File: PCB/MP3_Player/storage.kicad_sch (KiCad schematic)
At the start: 8 parts, among them J6 Micro_SD_Card

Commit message: Minor Schematic Changes
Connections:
- net DAT1: now also R19.2; no longer R17.2
- net DAT2: now also R17.2; no longer R19.2
- net SD_CMD: now also R20.1; no longer R21.1
- net SD_DAT0: now also R21.1; no longer R20.1
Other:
- moved on the sheet: C35, C36

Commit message: Started Making BOM
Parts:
- C35: Mfr. Part # (none) -> CL10A106KP8NNNC; Store URL - Digikey (none) -> https://www.digikey.pt/pt/products/detail/samsung-electro-m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; Store URL - Mouser (none) -> https://pt.mouser.com/en/ProductDetail/Samsung-Electro-Mech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
- C36: Mfr. Part # (none) -> CL05B104KP5NNNC; Store URL - Digikey (none) -> https://www.digikey.pt/pt/products/detail/samsung-electro-m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; Store URL - Mouser (none) -> https://pt.mouser.com/en/ProductDetail/Samsung-Electro-Mech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

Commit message: Continue Making BOM
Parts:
- R17, R18, R19, R20, R21: Mfr. Part # (none) -> CRCW040210K0FKED; Store URL - Digikey (none) -> https://www.digikey.pt/pt/products/detail/vishay-dale/CRCW0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; Store URL - Mouser (none) -> https://pt.mouser.com/en/ProductDetail/Vishay/CRCW040210K0F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
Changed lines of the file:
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@@
 			)
 		)
-		(property "Datasheet" ""
+		(property "Datasheet" "https://www.vishay.com/docs/20035/dcrcwe3.pdf"
 			(at 127 97.79 0)
 			(hide yes)
@@
 			)
 		)
-		(property "Description" "Resistor"
+		(property "Description" "0402"
 			(at 127 97.79 0)
 			(hide yes)
@@
 		)
 		(property "Store URL - TME" ""
+			(at 127 97.79 0)
+			(hide yes)
+			(show_name no)
+			(do_not_autoplace no)
+			(effects
+				(font
+					(size 1.27 1.27)
+				)
+			)
+		)
+		(property "Mfr. Part #" "CRCW040210K0FKED"
+			(at 127 97.79 0)
+			(hide yes)
+			(show_name no)
+			(do_not_autoplace no)
+			(effects
+				(font
+					(size 1.27 1.27)
+				)
+			)
+		)
+		(property "Store URL - Digikey" "https://www.digikey.pt/pt/products/detail/vishay-dale/CRCW040210K0FKED/1178121"
+			(at 127 97.79 0)
+			(hide yes)
+			(show_name no)
+			(do_not_autoplace no)
+			(effects
+				(font
+					(size 1.27 1.27)
+				)
+			)
+		)
+		(property "Store URL - Mouser" "https://pt.mouser.com/en/ProductDetail/Vishay/CRCW040210K0FKED?qs=rlE3Te1NifyN3e8vvxacSw%3D%3D"
 			(at 127 97.79 0)
 			(hide yes)
@@
 			)
 		)
-		(property "Datasheet" ""
+		(property "Datasheet" "https://www.vishay.com/docs/20035/dcrcwe3.pdf"
 			(at 182.88 105.41 0)
 			(hide yes)
@@
 			)
 		)
-		(property "Description" "Resistor"
+		(property "Description" "0402"
 			(at 182.88 105.41 0)
 			(hide yes)
@@
 		)
 		(property "Store URL - TME" ""
+			(at 182.88 105.41 90)
+			(hide yes)
+			(show_name no)
+			(do_not_autoplace no)
+			(effects
+				(font
+					(size 1.27 1.27)
+				)
+			)
+		)
+		(property "Mfr. Part #" "CRCW040210K0FKED"
+			(at 182.88 105.41 90)
+			(hide yes)
+			(show_name no)
+			(do_not_autoplace no)
+			(effects
+				(font
+					(size 1.27 1.27)
+				)
+			)
+		)
+		(property "Store URL - Digikey" "https://www.digikey.pt/pt/products/detail/vishay-dale/CRCW040210K0FKED/1178121"
+			(at 182.88 105.41 90)
+			(hide yes)
+			(show_name no)
+			(do_not_autoplace no)
+			(effects
+				(font
+					(size 1.27 1.27)
+				)
+			)
+		)
+		(property "Store URL - Mouser" "https://pt.mouser.com/en/ProductDetail/Vishay/CRCW040210K0FKED?qs=rlE3Te1NifyN3e8vvxacSw%3D%3D"
 			(at 182.88 105.41 90)
 			(hide yes)
@@
 			)
 		)
-		(property "Datasheet" ""
+		(property "Datasheet" "https://www.vishay.com/docs/20035/dcrcwe3.pdf"
 			(at 175.26 105.41 0)
 			(hide yes)
@@
 			)
 		)
-		(property "Description" "Resistor"
+		(property "Description" "0402"
 			(at 175.26 105.41 0)
 			(hide yes)
@@
 		)
 		(property "Store URL - TME" ""
+			(at 175.26 105.41 90)
+			(hide yes)
+			(show_name no)
+			(do_not_autoplace no)
+			(effects
+				(font
+					(size 1.27 1.27)
+				)
+			)
+		)
+		(property "Mfr. Part #" "CRCW040210K0FKED"
+			(at 175.26 105.41 90)
+			(hide yes)
+			(show_name no)
+			(do_not_autoplace no)
+			(effects
+				(font
+					(size 1.27 1.27)
+				)
+			)
+		)
+		(property "Store URL - Digikey" "https://www.digikey.pt/pt/products/detail/vishay-dale/CRCW040210K0FKED/1178121"
+			(at 175.26 105.41 90)
+			(hide yes)
+			(show_name no)
+			(do_not_autoplace no)
+			(effects
+				(font
+					(size 1.27 1.27)
+				)
+			)
+		)
+		(property "Store URL - Mouser" "https://pt.mouser.com/en/ProductDetail/Vishay/CRCW040210K0FKED?qs=rlE3Te1NifyN3e8vvxacSw%3D%3D"
 			(at 175.26 105.41 90)
 			(hide yes)
@@
 			)
 		)
-		(property "Datasheet" "https://www.we-online.com/components/products/datasheet/693072010801.pdf"
+		(property "Datasheet" ""
 			(at 153.67 71.12 0)
 			(hide yes)
@@
 			)
 		)
-		(property "Datasheet" ""
+		(property "Datasheet" "https://www.vishay.com/docs/20035/dcrcwe3.pdf"
 			(at 119.38 97.79 0)
 			(hide yes)
@@
 			)
 		)
-		(property "Description" "Resistor"
+		(property "Description" "0402"
 			(at 119.38 97.79 0)
 			(hide yes)
@@
 		)
 		(property "Store URL - TME" ""
+			(at 119.38 97.79 0)
+			(hide yes)
+			(show_name no)
+			(do_not_autoplace no)
+			(effects
+				(font
+					(size 1.27 1.27)
+				)
+			)
+		)
+		(property "Mfr. Part #" "CRCW040210K0FKED"
+			(at 119.38 97.79 0)
+			(hide yes)
+			(show_name no)
+			(do_not_autoplace no)
+			(effects
+				(font
+					(size 1.27 1.27)
+				)
+			)
+		)
+		(property "Store URL - Digikey" "https://www.digikey.pt/pt/products/detail/vishay-dale/CRCW040210K0FKED/1178121"
+			(at 119.38 97.79 0)
+			(hide yes)
+			(show_name no)
+			(do_not_autoplace no)
+			(effects
+				(font
+					(size 1.27 1.27)
+				)
+			)
+		)
+		(property "Store URL - Mouser" "https://pt.mouser.com/en/ProductDetail/Vishay/CRCW040210K0FKED?qs=rlE3Te1NifyN3e8vvxacSw%3D%3D"
 			(at 119.38 97.79 0)
 			(hide yes)
@@
 			)
 		)
-		(property "Datasheet" ""
+		(property "Datasheet" "https://www.vishay.com/docs/20035/dcrcwe3.pdf"
 			(at 190.5 105.41 0)
 			(hide yes)
@@
 			)
 		)
-		(property "Description" "Resistor"
+		(property "Description" "0402"
 			(at 190.5 105.41 0)
 			(hide yes)
@@
 			(at 190.5 105.41 90)
 			(hide yes)
+			(show_name no)
+			(do_not_autoplace no)
+			(effects
+				(font
+					(size 1.27 1.27)
+				)
+			)
+		)
+		(property "Mfr. Part #" "CRCW040210K0FKED"
+			(at 190.5 105.41 90)
+			(hide yes)
+			(show_name no)
+			(do_not_autoplace no)
+			(effects
+				(font
+					(size 1.27 1.27)
+				)
+			)
+		)
+		(property "Store URL - Digikey" "https://www.digikey.pt/pt/products/detail/vishay-dale/CRCW040210K0FKED/1178121"
+			(at 190.5 105.41 90)
+			(hide yes)
+			(show_name no)
+			(do_not_autoplace no)
+			(effects
+				(font
+					(size 1.27 1.27)
+				)
+			)
+		)
+		(property "Store URL - Mouser" "https://pt.mouser.com/en/ProductDetail/Vishay/CRCW040210K0FKED?qs=rlE3Te1NifyN3e8vvxacSw%3D%3D"
+			(at 190.5 105.41 90)
+			(hide yes)

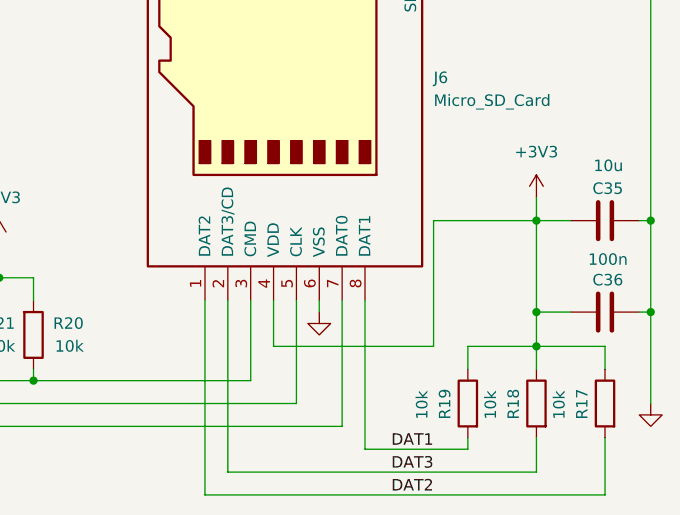
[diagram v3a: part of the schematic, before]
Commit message: Finished BOM; Started Footprint assignment
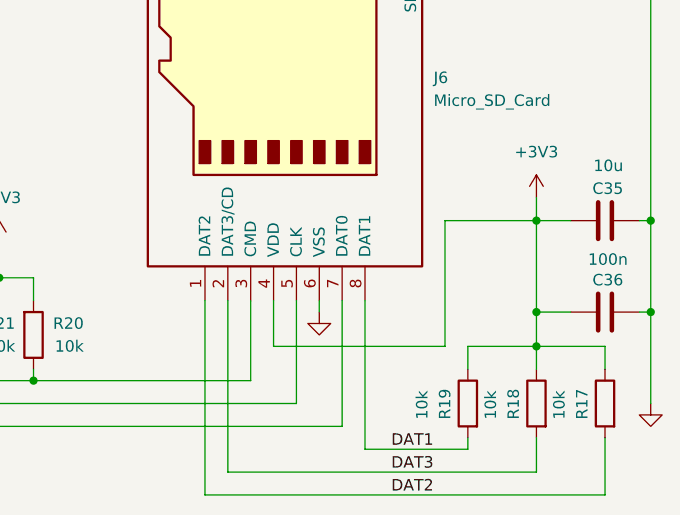
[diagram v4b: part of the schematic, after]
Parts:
- C35: footprint (none) -> Capacitor_SMD:C_0603_1608Metric
- C36, R17, R18, R19, R20, R21: footprint (none) -> Capacitor_SMD:C_0402_1005Metric
- J6: Mfr. Part # (none) -> MSD-1-A; Store URL - Digikey (none) -> https://www.digikey.pt/pt/products/detail/same-sky-formerly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; Store URL - Mouser (none) -> https://pt.mouser.com/en/ProductDetail/Same-Sky/MSD-1-A?qs=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
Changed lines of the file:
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@@
 	(wire
 		(pts
-			(xy 171.45 99.06) (xy 153.67 99.06)
+			(xy 172.72 99.06) (xy 153.67 99.06)
 		)
 		(stroke
@@
 	(wire
 		(pts
-			(xy 171.45 85.09) (xy 171.45 99.06)
+			(xy 172.72 85.09) (xy 172.72 99.06)
 		)
 		(stroke
@@
 	(wire
 		(pts
-			(xy 171.45 85.09) (xy 182.88 85.09)
+			(xy 172.72 85.09) (xy 182.88 85.09)
 		)
 		(stroke
@@
 			)
 		)
-		(property "Footprint" ""
+		(property "Footprint" "Capacitor_SMD:C_0402_1005Metric"
 			(at 125.222 97.79 90)
 			(hide yes)
@@
 			)
 		)
-		(property "Footprint" ""
+		(property "Footprint" "Capacitor_SMD:C_0402_1005Metric"
 			(at 184.658 105.41 90)
 			(hide yes)
@@
 			)
 		)
-		(property "Footprint" ""
+		(property "Footprint" "Capacitor_SMD:C_0603_1608Metric"
 			(at 194.31 86.0552 0)
 			(hide yes)
@@
 			)
 		)
-		(property "Footprint" ""
+		(property "Footprint" "Capacitor_SMD:C_0402_1005Metric"
 			(at 177.038 105.41 90)
 			(hide yes)
@@
 			)
 		)
-		(property "Datasheet" ""
+		(property "Datasheet" "https://www.cuidevices.com/product/resource/digikeypdf/msd-1-a.pdf"
 			(at 153.67 71.12 0)
 			(hide yes)
@@
 		)
 		(property "Store URL - TME" ""
+			(at 153.67 71.12 90)
+			(hide yes)
+			(show_name no)
+			(do_not_autoplace no)
+			(effects
+				(font
+					(size 1.27 1.27)
+				)
+			)
+		)
+		(property "Mfr. Part #" "MSD-1-A"
+			(at 153.67 71.12 90)
+			(hide yes)
+			(show_name no)
+			(do_not_autoplace no)
+			(effects
+				(font
+					(size 1.27 1.27)
+				)
+			)
+		)
+		(property "Store URL - Digikey" "https://www.digikey.pt/pt/products/detail/same-sky-formerly-cui-devices/MSD-1-A/21799641"
+			(at 153.67 71.12 90)
+			(hide yes)
+			(show_name no)
+			(do_not_autoplace no)
+			(effects
+				(font
+					(size 1.27 1.27)
+				)
+			)
+		)
+		(property "Store URL - Mouser" "https://pt.mouser.com/en/ProductDetail/Same-Sky/MSD-1-A?qs=sGAEpiMZZMvlX3nhDDO4AIrDL%2Fdv%252BVHxfeDZpUs0HoY%3D"
 			(at 153.67 71.12 90)
 			(hide yes)
@@
 			)
 		)
-		(property "Footprint" ""
+		(property "Footprint" "Capacitor_SMD:C_0402_1005Metric"
 			(at 194.31 96.2152 0)
 			(hide yes)
@@
 			)
 		)
-		(property "Footprint" ""
+		(property "Footprint" "Capacitor_SMD:C_0402_1005Metric"
 			(at 117.602 97.79 90)
 			(hide yes)
@@
 			)
 		)
-		(property "Footprint" ""
+		(property "Footprint" "Capacitor_SMD:C_0402_1005Metric"
 			(at 192.278 105.41 90)
 			(hide yes)

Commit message: Footprint Assingment
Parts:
- J6: footprint (none) -> MSD-1-A:CUI_MSD-1-A
- R17, R18, R19, R20, R21: footprint Capacitor_SMD:C_0402_1005Metric -> Resistor_SMD:R_0402_1005Metric
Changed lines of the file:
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@@
 			)
 		)
-		(property "Footprint" "Capacitor_SMD:C_0402_1005Metric"
+		(property "Footprint" "Resistor_SMD:R_0402_1005Metric"
 			(at 125.222 97.79 90)
 			(hide yes)
@@
 			)
 		)
-		(property "Footprint" "Capacitor_SMD:C_0402_1005Metric"
+		(property "Footprint" "Resistor_SMD:R_0402_1005Metric"
 			(at 184.658 105.41 90)
 			(hide yes)
@@
 			)
 		)
-		(property "Footprint" "Capacitor_SMD:C_0402_1005Metric"
+		(property "Footprint" "Resistor_SMD:R_0402_1005Metric"
 			(at 177.038 105.41 90)
 			(hide yes)
@@
 			)
 		)
-		(property "Footprint" ""
+		(property "Footprint" "MSD-1-A:CUI_MSD-1-A"
 			(at 146.05 41.91 0)
 			(hide yes)
@@
 			)
 		)
-		(property "Footprint" "Capacitor_SMD:C_0402_1005Metric"
+		(property "Footprint" "Resistor_SMD:R_0402_1005Metric"
 			(at 117.602 97.79 90)
 			(hide yes)
@@
 			)
 		)
-		(property "Footprint" "Capacitor_SMD:C_0402_1005Metric"
+		(property "Footprint" "Resistor_SMD:R_0402_1005Metric"
 			(at 192.278 105.41 90)
 			(hide yes)
